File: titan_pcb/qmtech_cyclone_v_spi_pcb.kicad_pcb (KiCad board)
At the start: 2 copper layers, 84.1 x 67.1 mm, 5 parts, among them J1 FPGA U8, J2 FPGA U7, J3 DUMMY_JTAG, U1 ESP32-DevKitC, U2 Teensy3.2

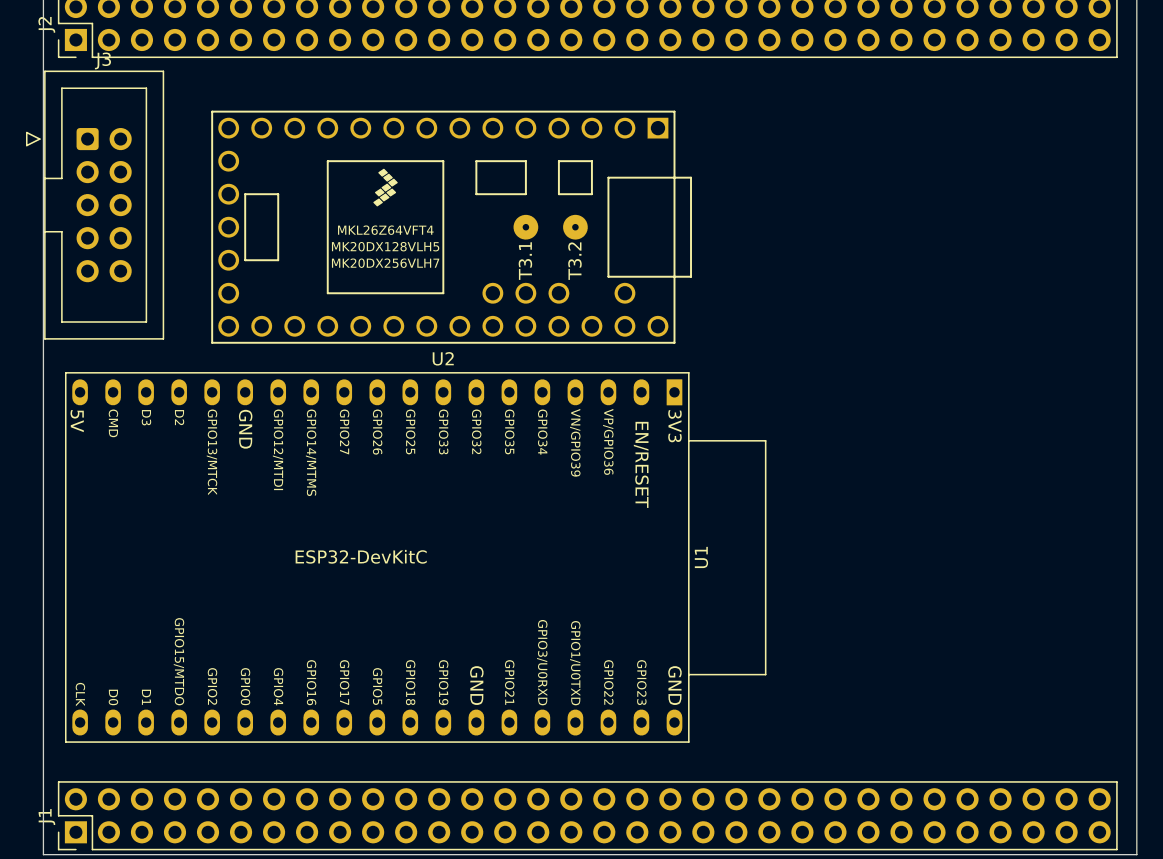
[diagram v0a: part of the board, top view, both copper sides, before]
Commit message: added pico to pcb
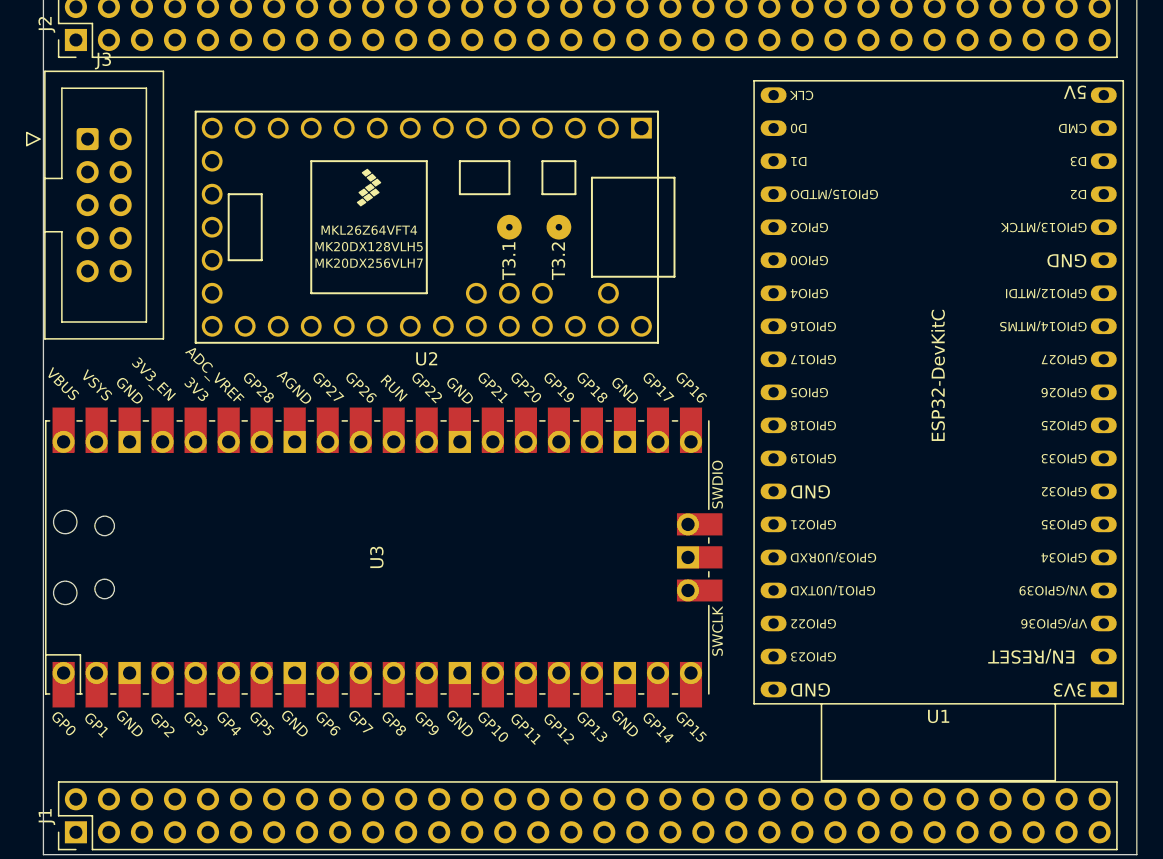
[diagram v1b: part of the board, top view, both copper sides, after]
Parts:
- added U3: Pico, MCU_RaspberryPi_and_Boards:RPi_Pico_SMD_TH, F.Cu at (50.8, 68.6)
- moved U1 40.2 mm to (106.7, 78.7), turned to 180 degrees
- moved U2 1.27 mm to (54.6, 43.2)

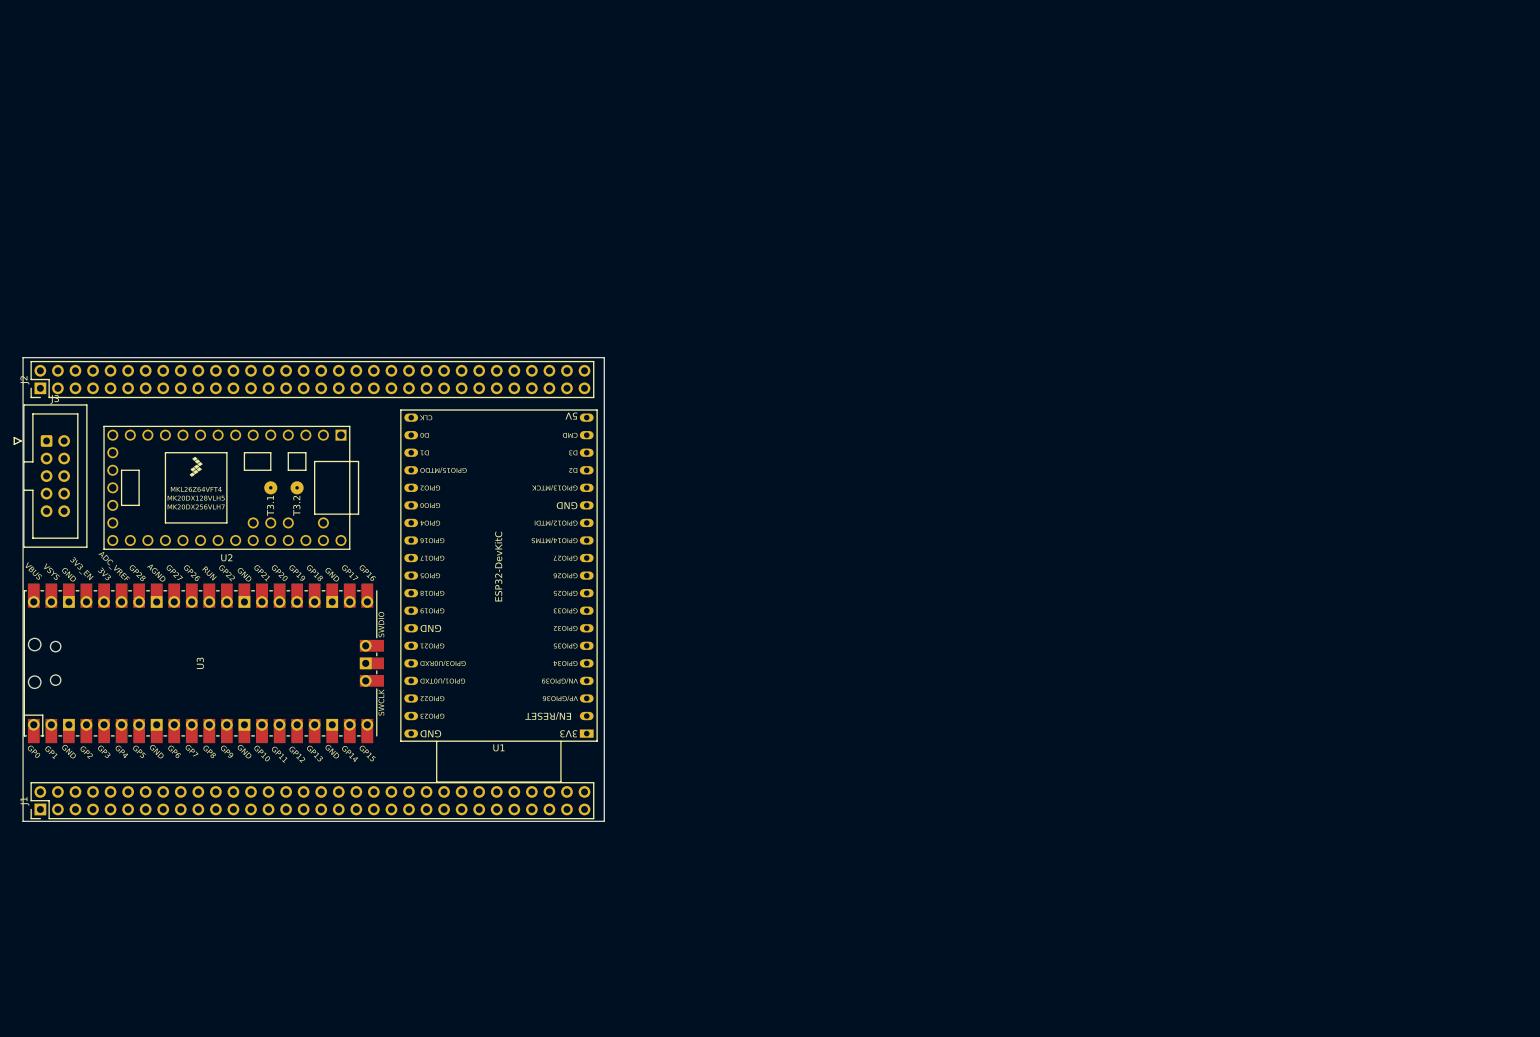
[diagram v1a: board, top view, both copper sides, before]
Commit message: basic board layout with pin assignments between MCUs and FPGA
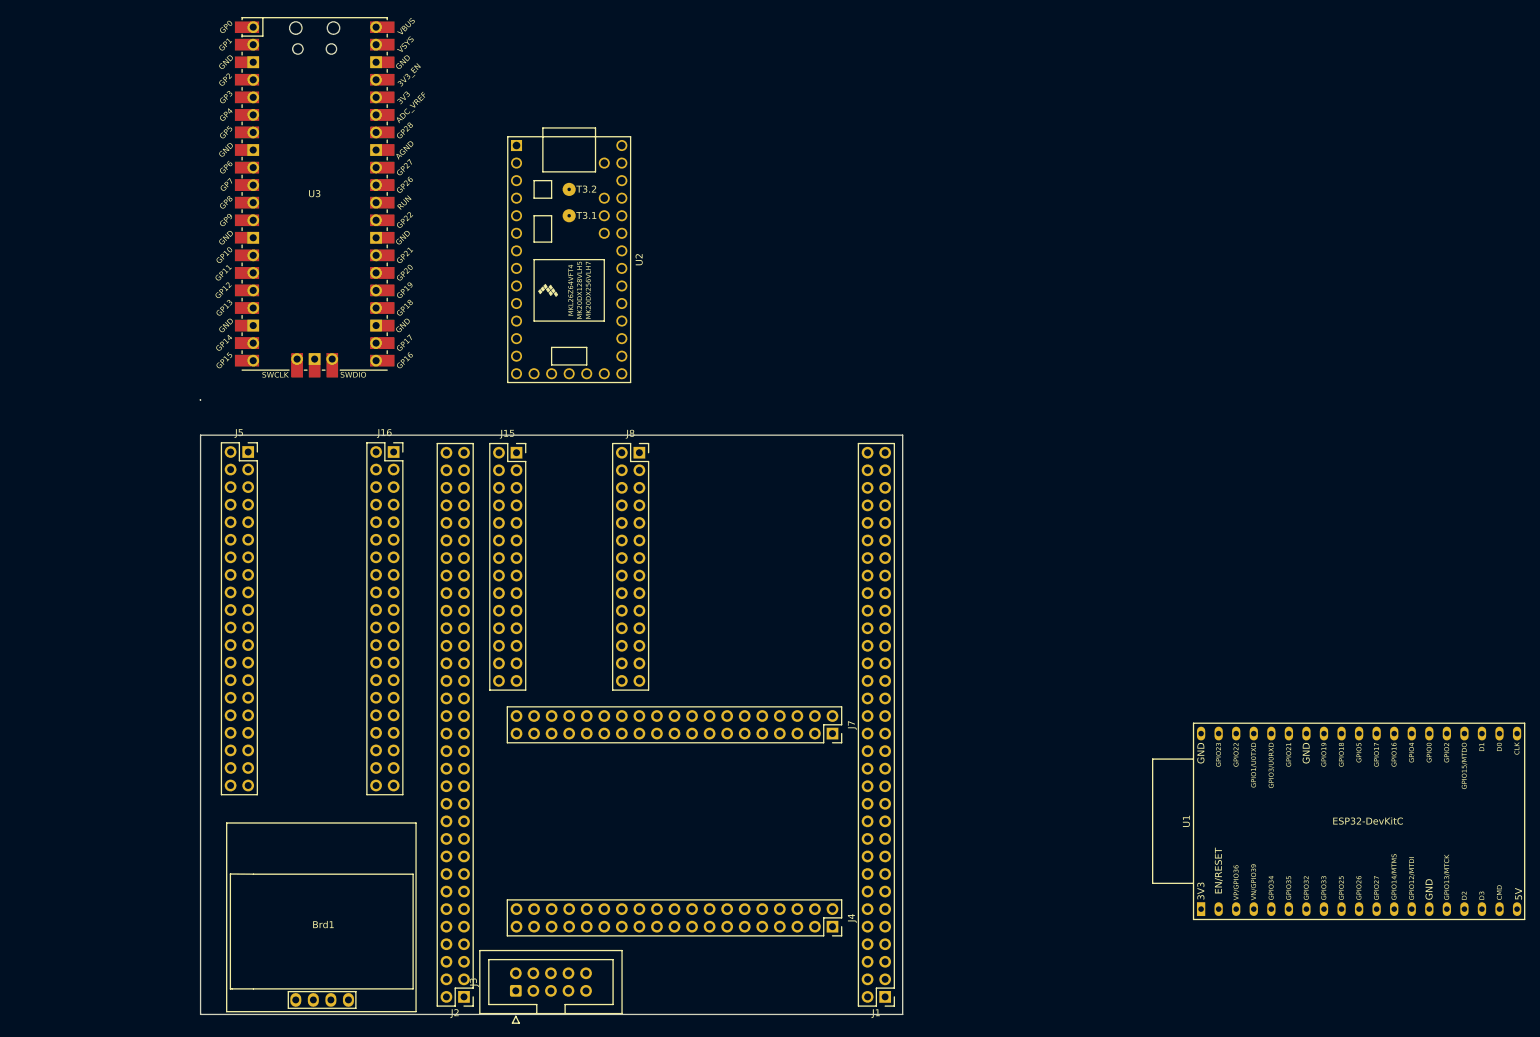
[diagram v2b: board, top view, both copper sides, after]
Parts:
- added Brd1: OLED, SSD1306:128x64OLED, F.Cu at (68.6, 106.7)
- added J15: teensy3.2_left_header_double, Connector_PinSocket_2.54mm:PinSocket_2x14_P2.54mm_Vertical, F.Cu at (96.5, 38.1)
- added J16: pico_right_header_double, Connector_PinSocket_2.54mm:PinSocket_2x20_P2.54mm_Vertical, F.Cu at (78.7, 38.0)
- added J4: esp_right_header_double, Connector_PinSocket_2.54mm:PinSocket_2x19_P2.54mm_Vertical, F.Cu at (142.2, 106.7)
- added J5: pico_left_header_double, Connector_PinSocket_2.54mm:PinSocket_2x20_P2.54mm_Vertical, F.Cu at (57.7, 38.0)
- added J7: esp_left_header_double, Connector_PinSocket_2.54mm:PinSocket_2x19_P2.54mm_Vertical, F.Cu at (142.2, 78.7)
- added J8: teensy3.2_right_header_double, Connector_PinSocket_2.54mm:PinSocket_2x14_P2.54mm_Vertical, F.Cu at (114.3, 38.1)
- moved J1 125.2 mm to (149.9, 116.8), turned to 180 degrees
- moved J2 107.3 mm to (88.9, 116.8), turned to 180 degrees
- moved J3 104.6 mm to (96.4, 116.0), turned to 90 degrees
- moved U1 92.5 mm to (195.6, 104.1), turned to 90 degrees
- moved U3 69.9 mm to (67.3, 0.65), turned to 0 degrees
- moved U2 59.5 mm to (104.1, 10.2), turned to -90 degrees
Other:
- board size 84.1 x 67.1 mm -> 101.6 x 88.9 mm
